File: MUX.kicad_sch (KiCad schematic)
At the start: 4 parts

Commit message: added more notes and documentation
todo:
    - timing analysis to make sure everything fits in 250nS + hold time/prep time
    - logic analysis to ensure correct functionality (am gonna make dumb mistakes!)
    - board layout
    - physical testing!
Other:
- note removed: "THE MEMORY ADDRESS SPACE IS BROKEN UP INTO 4 "PAGES" OF 16K. THE FRST 4 PAGES OF SPACE DIRECTLY CORRESPOND TO THE EXISTING HARDWARE. FOR EACH MEMORY ACCESS WE DETERMINE USING THE MAPPER HARDWARE WHICH ONE OF 4 PAGE REGISTERS TO PLACE ON THE BANK BUS (IBB)."
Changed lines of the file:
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@@
     (rev "1030211022")
     (company "LISTOFOPTIONS")
+    (comment 1 "the selector mux here determines which set page the processor is accessing")
+    (comment 2 "pages 0..3 are system default pages, 4..127 are rom, and 128..256 are ram")
+    (comment 3 "there are 256 pages of memory, each assignable to one of the 4 sections")
+    (comment 4 "memory is broken up into 4 sections of 16k (AB_{15}..AB_{14} determine page requested)")
   )
   (bus_entry (at 223.52 76.2) (size -2.54 2.54)
@@
     (stroke (width 0) (type default) (color 0 0 0 0))
   )
-  (text "THE MEMORY ADDRESS SPACE IS BROKEN UP INTO 4 \"PAGES\" OF 16K.\nTHE FRST 4 PAGES OF SPACE DIRECTLY CORRESPOND TO THE\nEXISTING HARDWARE. FOR EACH MEMORY ACCESS WE DETERMINE USING\nTHE MAPPER HARDWARE WHICH ONE OF 4 PAGE REGISTERS TO PLACE ON\nTHE BANK BUS (IBB). "
-    (at 176.53 166.37 0)
-    (effects (font (size 1.27 1.27)) (justify left bottom))
-  )
   (label "AB_{3}" (at 193.04 81.28 0)

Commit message: changed bus names to avoid possible conflicts, fixed unnamed busses.
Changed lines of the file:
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@@
     (effects (font (size 1.27 1.27)) (justify left bottom))
-  )
-  (label "PAB_{4}_{[0..7]}" (at 124.46 88.9 270)
-    (effects (font (size 1.27 1.27)) (justify right bottom))
   )
   (label "EAB_{8}" (at 220.98 93.98 180)
@@
     (effects (font (size 1.27 1.27)) (justify right bottom))
   )
-  (label "PAB_{3}_{[0..7]}" (at 31.75 88.9 270)
-    (effects (font (size 1.27 1.27)) (justify right bottom))
-  )
-  (label "PAB_{2}_{[0..7]}" (at 116.84 88.9 270)
-    (effects (font (size 1.27 1.27)) (justify right bottom))
-  )
-  (label "PAB_{1}_{[0..7]}" (at 113.03 88.9 270)
-    (effects (font (size 1.27 1.27)) (justify right bottom))
-  )
   (label "IBB_{3}" (at 182.88 121.92 0)
     (effects (font (size 1.27 1.27)) (justify left bottom))
@@
     (effects (font (size 1.27 1.27)) (justify right bottom))
   )
-  (label "PAB_{4}_{[0..7]}" (at 35.56 88.9 270)
-    (effects (font (size 1.27 1.27)) (justify right bottom))
-  )
   (label "PAB_{2}_{7}" (at 139.7 137.16 180)
     (effects (font (size 1.27 1.27)) (justify right bottom))
@@
     (effects (font (size 1.27 1.27)) (justify left bottom))
   )
-  (label "PAB_{3}_{[0..7]}" (at 120.65 88.9 270)
-    (effects (font (size 1.27 1.27)) (justify right bottom))
-  )
   (label "EAB_{20}" (at 220.98 129.54 180)
     (effects (font (size 1.27 1.27)) (justify right bottom))
@@
     (effects (font (size 1.27 1.27)) (justify right bottom))
   )
-  (label "PAB_{2}_{[0..7]}" (at 27.94 88.9 270)
-    (effects (font (size 1.27 1.27)) (justify right bottom))
-  )
   (label "PAB_{1}_{4}" (at 50.8 121.92 180)
     (effects (font (size 1.27 1.27)) (justify right bottom))
@@
     (effects (font (size 1.27 1.27)) (justify right bottom))
   )
-  (label "PAB_{1}_{[0..7]}" (at 24.13 88.9 270)
-    (effects (font (size 1.27 1.27)) (justify right bottom))
-  )
   (label "EAB_{18}" (at 220.98 124.46 180)
     (effects (font (size 1.27 1.27)) (justify right bottom))
@@
     (effects (font (size 1.27 1.27)) (justify left bottom))
   )
-  (hierarchical_label "PAN_{4}_{[0..7]}" (shape input) (at 35.56 35.56 90)
+  (hierarchical_label "PAB_{4}_{[0..7]}" (shape input) (at 35.56 35.56 90)
     (effects (font (size 1.27 1.27)) (justify left))
   )
@@
     (effects (font (size 1.27 1.27)) (justify left))
   )
-  (hierarchical_label "PAN_{1}_{[0..7]}" (shape input) (at 24.13 43.18 90)
+  (hierarchical_label "PAB_{1}_{[0..7]}" (shape input) (at 24.13 43.18 90)
     (effects (font (size 1.27 1.27)) (justify left))
   )
@@
     (effects (font (size 1.27 1.27)) (justify left))
   )
-  (hierarchical_label "PAN_{2}_{[0..7]}" (shape input) (at 27.94 40.64 90)
-    (effects (font (size 1.27 1.27)) (justify left))
-  )
-  (hierarchical_label "PAN_{3}_{[0..7]}" (shape input) (at 31.75 38.1 90)
-    (effects (font (size 1.27 1.27)) (justify left))
-  )
+  (hierarchical_label "PAB_{2}_{[0..7]}" (shape input) (at 27.94 40.64 90)
+    (effects (font (size 1.27 1.27)) (justify left))
+  )
+  (hierarchical_label "PAB_{3}_{[0..7]}" (shape input) (at 31.75 38.1 90)
+    (effects (font (size 1.27 1.27)) (justify left))
+  )

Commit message: added decoupling capacitors, perhaps too many? idk better more than less!
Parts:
- added C? (x4): 0U1, symbol Device:C_Small
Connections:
- net +5V: now also C?.1, C?.1, C?.1, C?.1
- net GNDD: now also C?.2, C?.2, C?.2, C?.2
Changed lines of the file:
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@@
     (effects (font (size 1.27 1.27)) (justify left))
+  )
+  (symbol (lib_id "power:+5V") (at 162.56 78.74 0) (unit 1)
+    (in_bom yes) (on_board yes) (fields_autoplaced)
+    (property "Reference" "#PWR?" (id 0) (at 162.56 82.55 0)
+      (effects (font (size 1.27 1.27)) hide)
+    )
+    (property "Value" "+5V" (id 1) (at 162.56 73.025 0))
+    (property "Footprint" "" (id 2) (at 162.56 78.74 0)
+      (effects (font (size 1.27 1.27)) hide)
+    )
+    (property "Datasheet" "" (id 3) (at 162.56 78.74 0)
+      (effects (font (size 1.27 1.27)) hide)
+    )
+    (pin "1")
+  )
+  (symbol (lib_id "Device:C_Small") (at 162.56 157.48 0) (unit 1)
+    (in_bom yes) (on_board yes) (fields_autoplaced)
+    (property "Reference" "C?" (id 0) (at 165.1 156.2162 0)
+      (effects (font (size 1.27 1.27)) (justify left))
+    )
+    (property "Value" "0U1" (id 1) (at 165.1 158.7562 0)
+      (effects (font (size 1.27 1.27)) (justify left))
+    )
+    (property "Footprint" "" (id 2) (at 162.56 157.48 0)
+      (effects (font (size 1.27 1.27)) hide)
+    )
+    (property "Datasheet" "~" (id 3) (at 162.56 157.48 0)
+      (effects (font (size 1.27 1.27)) hide)
+    )
+    (pin "1")
+    (pin "2")
   )
   (symbol (lib_id "power:+5V") (at 152.4 106.68 0) (unit 1)
@@
     (pin "9")
   )
+  (symbol (lib_id "power:GNDD") (at 73.66 83.82 0) (unit 1)
+    (in_bom yes) (on_board yes) (fields_autoplaced)
+    (property "Reference" "#PWR?" (id 0) (at 73.66 90.17 0)
+      (effects (font (size 1.27 1.27)) hide)
+    )
+    (property "Value" "GNDD" (id 1) (at 73.66 88.265 0))
+    (property "Footprint" "" (id 2) (at 73.66 83.82 0)
+      (effects (font (size 1.27 1.27)) hide)
+    )
+    (property "Datasheet" "" (id 3) (at 73.66 83.82 0)
+      (effects (font (size 1.27 1.27)) hide)
+    )
+    (pin "1")
+  )
   (symbol (lib_id "power:GNDD") (at 139.7 144.78 270) (unit 1)
     (in_bom yes) (on_board yes) (fields_autoplaced)
@@
     )
     (pin "1")
+  )
+  (symbol (lib_id "Device:C_Small") (at 162.56 81.28 0) (unit 1)
+    (in_bom yes) (on_board yes) (fields_autoplaced)
+    (property "Reference" "C?" (id 0) (at 165.1 80.0162 0)
+      (effects (font (size 1.27 1.27)) (justify left))
+    )
+    (property "Value" "0U1" (id 1) (at 165.1 82.5562 0)
+      (effects (font (size 1.27 1.27)) (justify left))
+    )
+    (property "Footprint" "" (id 2) (at 162.56 81.28 0)
+      (effects (font (size 1.27 1.27)) hide)
+    )
+    (property "Datasheet" "~" (id 3) (at 162.56 81.28 0)
+      (effects (font (size 1.27 1.27)) hide)
+    )
+    (pin "1")
+    (pin "2")
   )
   (symbol (lib_id "74xx:74LS153") (at 152.4 132.08 0) (unit 1)
@@
     (pin "9")
   )
+  (symbol (lib_id "Device:C_Small") (at 73.66 157.48 0) (unit 1)
+    (in_bom yes) (on_board yes) (fields_autoplaced)
+    (property "Reference" "C?" (id 0) (at 76.2 156.2162 0)
+      (effects (font (size 1.27 1.27)) (justify left))
+    )
+    (property "Value" "0U1" (id 1) (at 76.2 158.7562 0)
+      (effects (font (size 1.27 1.27)) (justify left))
+    )
+    (property "Footprint" "" (id 2) (at 73.66 157.48 0)
+      (effects (font (size 1.27 1.27)) hide)
+    )
+    (property "Datasheet" "~" (id 3) (at 73.66 157.48 0)
+      (effects (font (size 1.27 1.27)) hide)
+    )
+    (pin "1")
+    (pin "2")
+  )
   (symbol (lib_id "74xx:74LS153") (at 63.5 132.08 0) (unit 1)
     (in_bom yes) (on_board yes) (fields_autoplaced)
@@
     (pin "1")
   )
+  (symbol (lib_id "power:+5V") (at 73.66 78.74 0) (unit 1)
+    (in_bom yes) (on_board yes) (fields_autoplaced)
+    (property "Reference" "#PWR?" (id 0) (at 73.66 82.55 0)
+      (effects (font (size 1.27 1.27)) hide)
+    )
+    (property "Value" "+5V" (id 1) (at 73.66 73.025 0))
+    (property "Footprint" "" (id 2) (at 73.66 78.74 0)
+      (effects (font (size 1.27 1.27)) hide)
+    )
+    (property "Datasheet" "" (id 3) (at 73.66 78.74 0)
+      (effects (font (size 1.27 1.27)) hide)
+    )
+    (pin "1")
+  )
+  (symbol (lib_id "power:GNDD") (at 73.66 160.02 0) (unit 1)
+    (in_bom yes) (on_board yes) (fields_autoplaced)
+    (property "Reference" "#PWR?" (id 0) (at 73.66 166.37 0)
+      (effects (font (size 1.27 1.27)) hide)
+    )
+    (property "Value" "GNDD" (id 1) (at 73.66 164.465 0))
+    (property "Footprint" "" (id 2) (at 73.66 160.02 0)
+      (effects (font (size 1.27 1.27)) hide)
+    )
+    (property "Datasheet" "" (id 3) (at 73.66 160.02 0)
+      (effects (font (size 1.27 1.27)) hide)
+    )
+    (pin "1")
+  )
+  (symbol (lib_id "Device:C_Small") (at 73.66 81.28 0) (unit 1)
+    (in_bom yes) (on_board yes) (fields_autoplaced)
+    (property "Reference" "C?" (id 0) (at 76.2 80.0162 0)
+      (effects (font (size 1.27 1.27)) (justify left))
+    )
+    (property "Value" "0U1" (id 1) (at 76.2 82.5562 0)
+      (effects (font (size 1.27 1.27)) (justify left))
+    )
+    (property "Footprint" "" (id 2) (at 73.66 81.28 0)
+      (effects (font (size 1.27 1.27)) hide)
+    )
+    (property "Datasheet" "~" (id 3) (at 73.66 81.28 0)
+      (effects (font (size 1.27 1.27)) hide)
+    )
+    (pin "1")
+    (pin "2")
+  )
   (symbol (lib_id "power:GNDD") (at 139.7 50.8 270) (unit 1)
     (in_bom yes) (on_board yes) (fields_autoplaced)
@@
     )
     (property "Datasheet" "" (id 3) (at 139.7 50.8 0)
+      (effects (font (size 1.27 1.27)) hide)
+    )
+    (pin "1")
+  )
+  (symbol (lib_id "power:GNDD") (at 162.56 160.02 0) (unit 1)
+    (in_bom yes) (on_board yes) (fields_autoplaced)
+    (property "Reference" "#PWR?" (id 0) (at 162.56 166.37 0)
+      (effects (font (size 1.27 1.27)) hide)
+    )
+    (property "Value" "GNDD" (id 1) (at 162.56 164.465 0))
+    (property "Footprint" "" (id 2) (at 162.56 160.02 0)
+      (effects (font (size 1.27 1.27)) hide)
+    )
+    (property "Datasheet" "" (id 3) (at 162.56 160.02 0)
       (effects (font (size 1.27 1.27)) hide)
     )
@@
       (effects (font (size 1.27 1.27)) hide)
     )
+    (pin "1")
+  )
+  (symbol (lib_id "power:GNDD") (at 162.56 83.82 0) (unit 1)
+    (in_bom yes) (on_board yes) (fields_autoplaced)
+    (property "Reference" "#PWR?" (id 0) (at 162.56 90.17 0)
+      (effects (font (size 1.27 1.27)) hide)
+    )
+    (property "Value" "GNDD" (id 1) (at 162.56 88.265 0))
+    (property "Footprint" "" (id 2) (at 162.56 83.82 0)
+      (effects (font (size 1.27 1.27)) hide)
+    )
+    (property "Datasheet" "" (id 3) (at 162.56 83.82 0)
+      (effects (font (size 1.27 1.27)) hide)
+    )
+    (pin "1")
+  )
+  (symbol (lib_id "power:+5V") (at 73.66 154.94 0) (unit 1)
+    (in_bom yes) (on_board yes) (fields_autoplaced)
+    (property "Reference" "#PWR?" (id 0) (at 73.66 158.75 0)
+      (effects (font (size 1.27 1.27)) hide)
+    )
+    (property "Value" "+5V" (id 1) (at 73.66 149.225 0))
+    (property "Footprint" "" (id 2) (at 73.66 154.94 0)
+      (effects (font (size 1.27 1.27)) hide)
+    )
+    (property "Datasheet" "" (id 3) (at 73.66 154.94 0)
+      (effects (font (size 1.27 1.27)) hide)
+    )
+    (pin "1")
+  )
+  (symbol (lib_id "power:+5V") (at 162.56 154.94 0) (unit 1)
+    (in_bom yes) (on_board yes) (fields_autoplaced)
+    (property "Reference" "#PWR?" (id 0) (at 162.56 158.75 0)
+      (effects (font (size 1.27 1.27)) hide)
+    )
+    (property "Value" "+5V" (id 1) (at 162.56 149.225 0))
+    (property "Footprint" "" (id 2) (at 162.56 154.94 0)
+      (effects (font (size 1.27 1.27)) hide)
+    )
+    (property "Datasheet" "" (id 3) (at 162.56 154.94 0)
+      (effects (font (size 1.27 1.27)) hide)
+    )

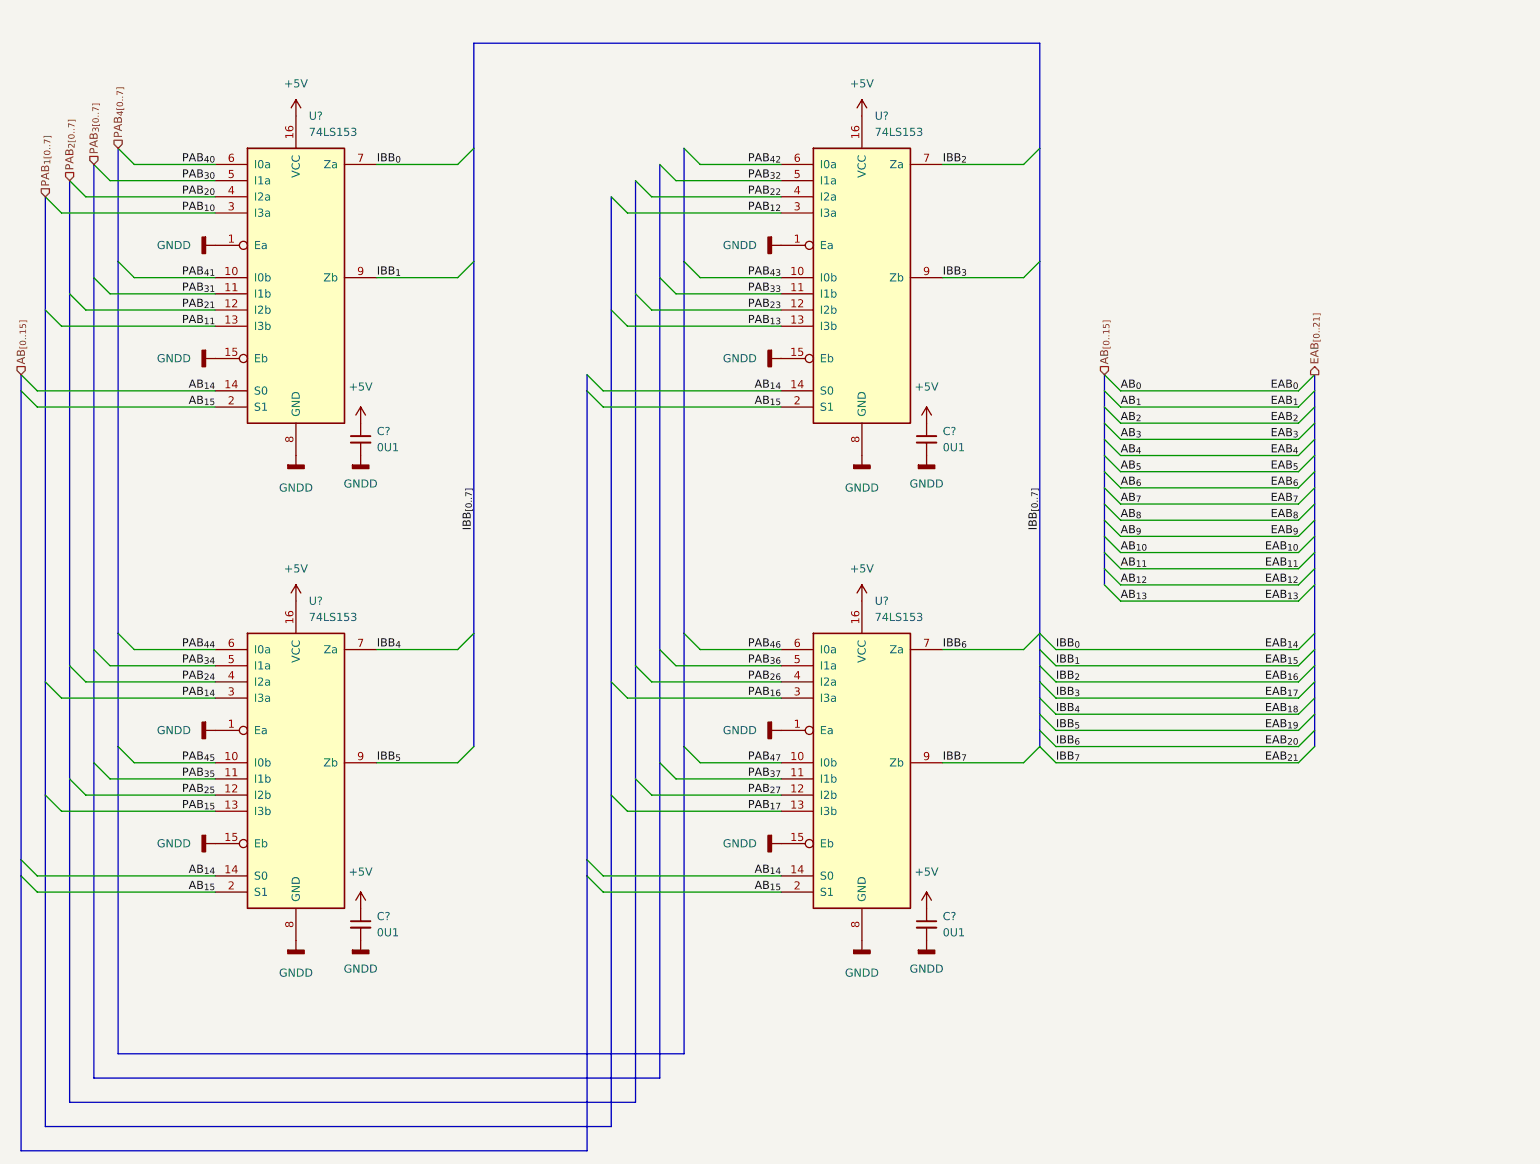
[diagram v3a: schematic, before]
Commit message: some clean up and simplification, as well as some renaming
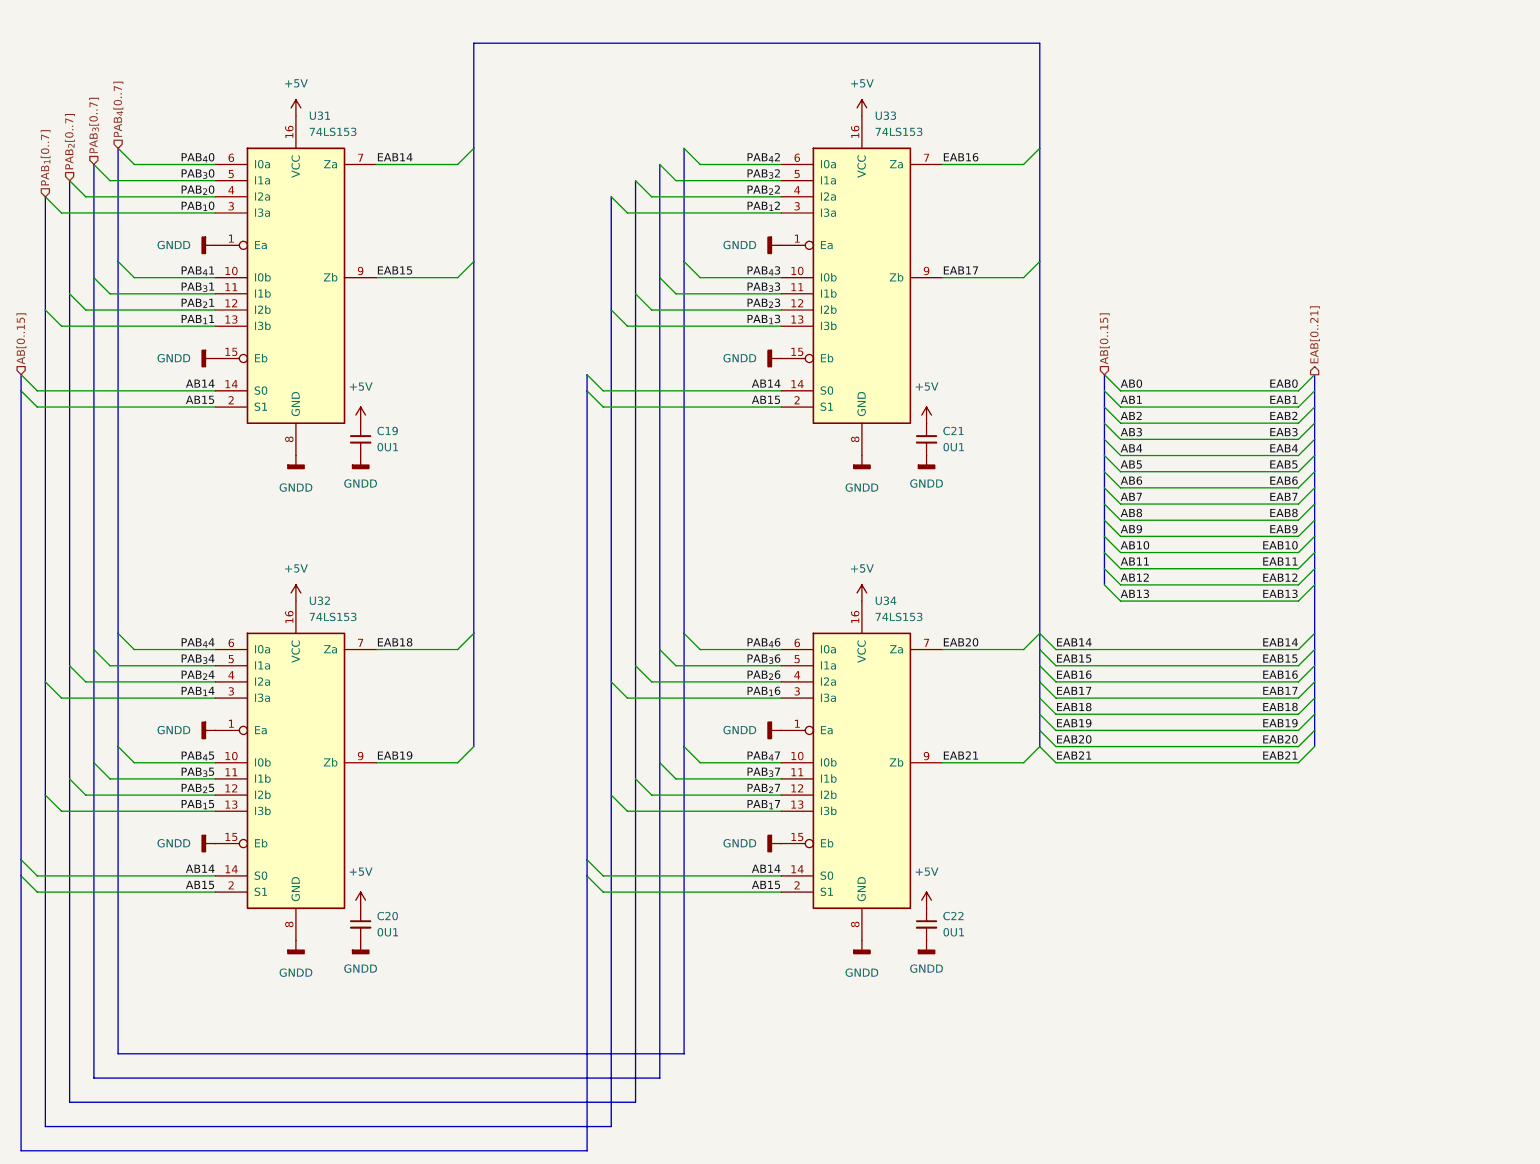
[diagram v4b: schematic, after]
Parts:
- gave numbers to parts that had none: 8
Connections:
- net AB_{14} renamed AB14
- net AB_{15} renamed AB15
- net EAB_{14} renamed EAB14
- net EAB_{15} renamed EAB15
- net EAB_{16} renamed EAB16
- net EAB_{17} renamed EAB17
- net EAB_{18} renamed EAB18
- net EAB_{19} renamed EAB19
- net EAB_{20} renamed EAB20
- net EAB_{21} renamed EAB21
- net PAB_{1}_{0} renamed PAB_{1}0
- net PAB_{1}_{1} renamed PAB_{1}1
- net PAB_{1}_{2} renamed PAB_{1}2
- net PAB_{1}_{3} renamed PAB_{1}3
- net PAB_{1}_{4} renamed PAB_{1}4
- net PAB_{1}_{5} renamed PAB_{1}5
- net PAB_{1}_{6} renamed PAB_{1}6
- net PAB_{1}_{7} renamed PAB_{1}7
- net PAB_{2}_{0} renamed PAB_{2}0
- net PAB_{2}_{1} renamed PAB_{2}1
- net PAB_{2}_{2} renamed PAB_{2}2
- net PAB_{2}_{3} renamed PAB_{2}3
- net PAB_{2}_{4} renamed PAB_{2}4
- net PAB_{2}_{5} renamed PAB_{2}5
- net PAB_{2}_{6} renamed PAB_{2}6
- net PAB_{2}_{7} renamed PAB_{2}7
- net PAB_{3}_{0} renamed PAB_{3}0
- net PAB_{3}_{1} renamed PAB_{3}1
- net PAB_{3}_{2} renamed PAB_{3}2
- net PAB_{3}_{3} renamed PAB_{3}3
- net PAB_{3}_{4} renamed PAB_{3}4
- net PAB_{3}_{5} renamed PAB_{3}5
- net PAB_{3}_{6} renamed PAB_{3}6
- net PAB_{3}_{7} renamed PAB_{3}7
- net PAB_{4}_{0} renamed PAB_{4}0
- net PAB_{4}_{1} renamed PAB_{4}1
- net PAB_{4}_{2} renamed PAB_{4}2
- net PAB_{4}_{3} renamed PAB_{4}3
- net PAB_{4}_{4} renamed PAB_{4}4
- net PAB_{4}_{5} renamed PAB_{4}5
- net PAB_{4}_{6} renamed PAB_{4}6
- net PAB_{4}_{7} renamed PAB_{4}7
